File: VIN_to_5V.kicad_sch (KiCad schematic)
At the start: 3 parts, among them U5 AMS1117-5.0

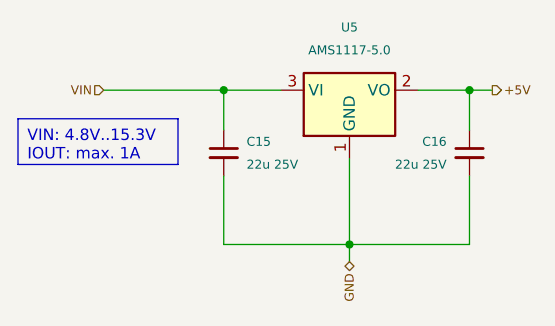
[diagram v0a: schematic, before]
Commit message: Replace 3V3 LDO for a 1A model
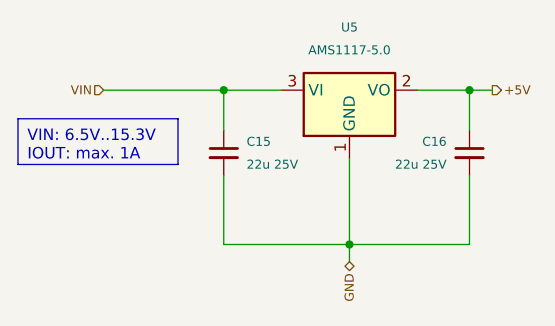
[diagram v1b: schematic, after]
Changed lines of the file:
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@@
     (stroke (width 0) (type default))
   )
-  (text_box "VIN: 4.8V..15.3V\nIOUT: max. 1A"
+  (text_box "VIN: 6.5V..15.3V\nIOUT: max. 1A"
     (at 40.005 55.88 0) (size 17.78 5.08)
     (stroke (width 0) (type default))
